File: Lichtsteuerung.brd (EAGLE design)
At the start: 157.7 x 86.4 mm, 180 parts, among them IC1 74HC595D, IC10 TSR_1-2450, IC11 MEGA64-A, IC12 75176AD, IC13 DS1307SO8, IC2 74HC595D, IC3 74HC595D, IC4 74HC595D, IC5 75176AD, IC6 MEGA8-AI, IC9 24FC128-I/SN, Q1 32.768, Q2 16MHz, Q3 16MHz, U1 MAX232SOIC16, X1 713-1410, X2 713-1410, X3 733-333, X5 713-1410, X6 733-334, X7 733-333, X8 733-333

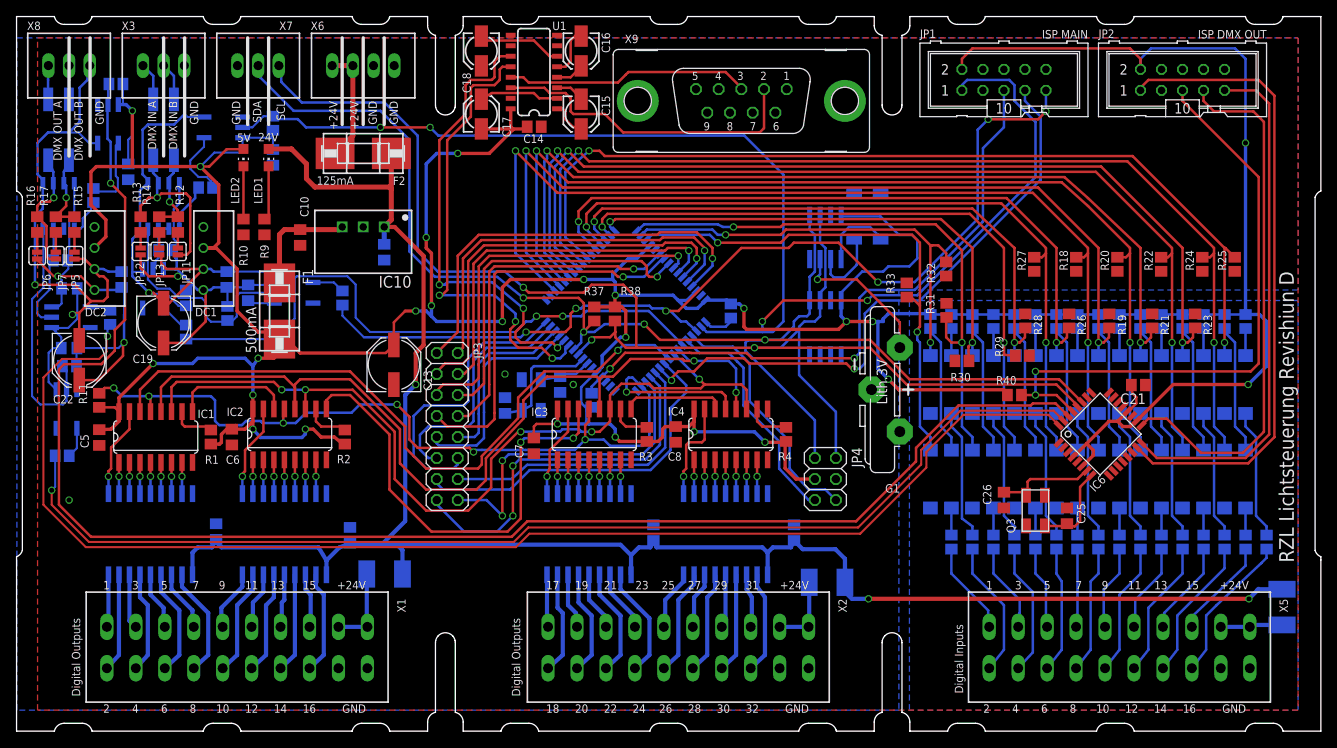
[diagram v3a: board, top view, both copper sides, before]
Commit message: Re-added smd jumpers, fixed silkscreens and added a few test points
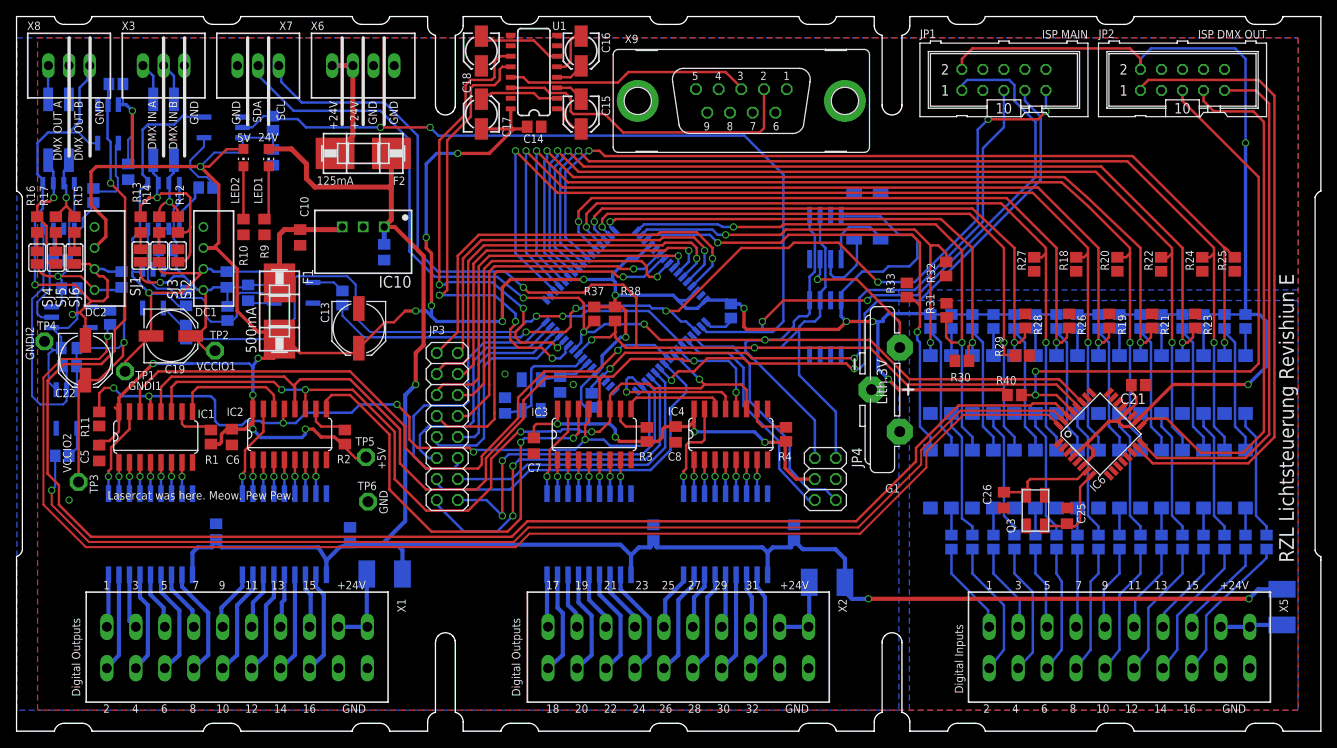
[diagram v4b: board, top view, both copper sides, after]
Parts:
- removed JP11, JP12, JP13, JP5, JP6, JP7: (no value), SparkFun:SJ_2S
- added SJ1, SJ2, SJ3, SJ4, SJ5, SJ6: (no value), jumper:SJ
- added TP1, TP2, TP3, TP4, TP5, TP6: TPPAD1-13, testpad:P1-13
- moved C13 6.11 mm to (41.4, 48.7), turned to 270 degrees
- moved R11 2.25 mm to (10.0, 37.8)
- moved C5 1.88 mm to (10.0, 33.6)
- moved C19 1.79 mm to (18.7, 47.8), turned to 0 degrees
- moved C22 0.75 mm to (8.33, 44.8)
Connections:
- removed net N$53: IC12.6, JP11.1, L1.1, R13.1
- removed net N$77: IC5.6, JP7.1, L2.1, R16.1
- removed net N$85: JP12.2, R13.2
- removed net N$86: JP13.1, R14.1
- removed net N$89: JP11.2, R12.1
- removed net N$91: JP5.1, R15.2
- removed net N$92: JP7.2, R17.1
- removed net N$94: JP6.2, R16.2
- new net TERM_A1: IC12.6, L1.1, R12.1, R13.1, SJ2.1
- new net TERM_A2: IC5.6, L2.1, R16.1, SJ5.1
- new net TERM_B1: SJ2.2
- new net TERM_B2: R17.1, SJ5.2
- new net TERM_HI1: R13.2, SJ1.2
- new net TERM_HI2: R16.2, SJ4.2
- new net TERM_LO1: R14.1, SJ3.2
- new net TERM_LO2: R15.2, SJ6.2
- net +5V: now also TP5.TP
- net GND: now also TP6.TP
- net GNDI1: now also SJ3.1, TP1.TP; no longer JP13.2
- net GNDI2: now also SJ6.1, TP4.TP; no longer JP5.2
- net VCCIO1: now also SJ1.1, TP2.TP; no longer JP12.1
- net VCCIO2: now also SJ4.1, TP3.TP; no longer JP6.1
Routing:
- net TERM_A1: track 0.00 -> 23.3 mm, vias 0 -> 1
- net N$53: track 21.2 -> 0.00 mm, vias 1 -> 0
- net TERM_A2: track 0.00 -> 15.5 mm, vias 0 -> 1
- net N$77: track 14.9 -> 0.00 mm, vias 1 -> 0
- net VCCIO2: track 55.5 -> 67.7 mm
- net GNDI1: track 76.5 -> 86.4 mm
- net N$94: track 2.39 -> 0.00 mm
- net N$92: track 2.39 -> 0.00 mm
- net N$91: track 2.39 -> 0.00 mm
- net TERM_LO2: track 0.00 -> 2.29 mm
- net TERM_HI2: track 0.00 -> 2.29 mm
- net TERM_B2: track 0.00 -> 2.29 mm
- net OE: track 108.6 -> 110.9 mm
- net TERM_LO1: track 0.00 -> 2.04 mm
- net TERM_HI1: track 0.00 -> 2.04 mm
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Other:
- board text added: "+5V"
- board text added: "GNDI1"
- board text added: "GNDI2"
- board text added: "Lasercat was here. Meow. Pew Pew."
- board text added: "RZL Lichtsteuerung Revishiun E"
- board text added: "VCCIO1"
- board text added: "VCCIO2"
- board text removed: "RZL Lichtsteuerung Revishiun D"

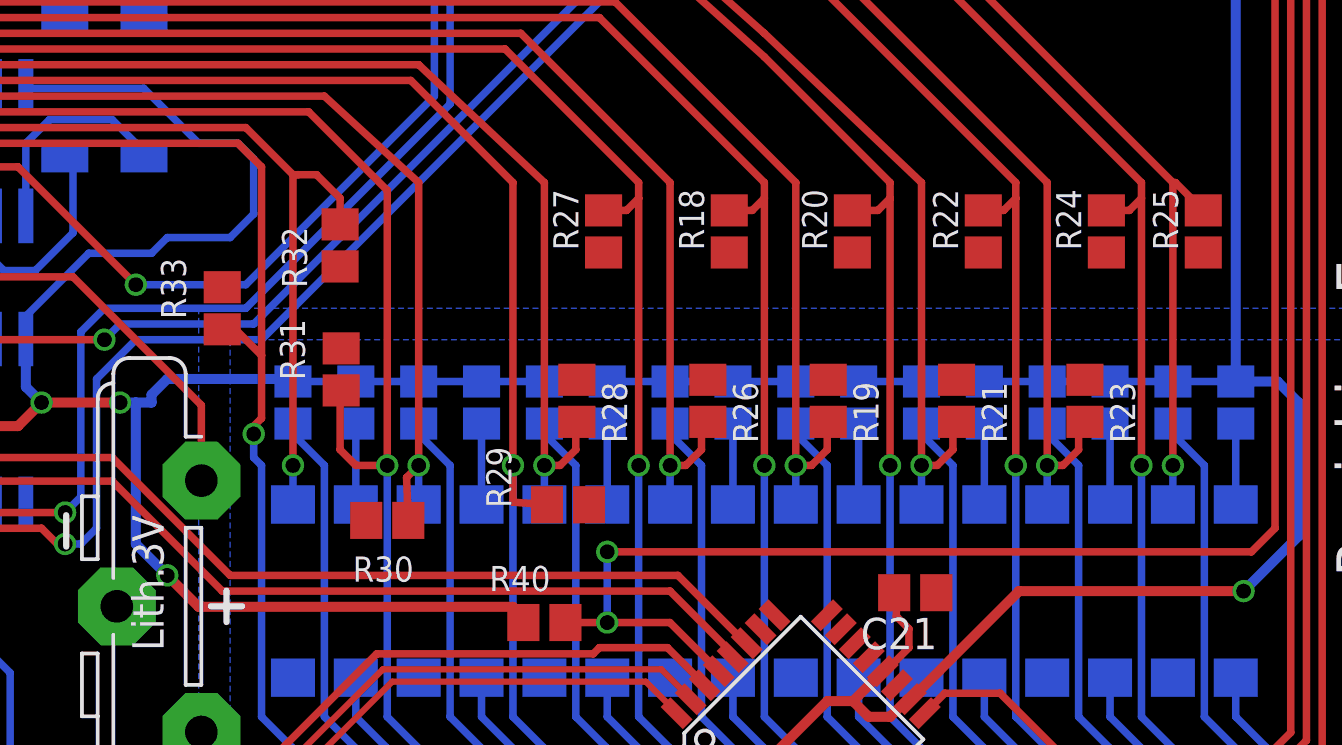
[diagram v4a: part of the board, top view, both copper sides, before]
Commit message: Added reichelt ordercodes
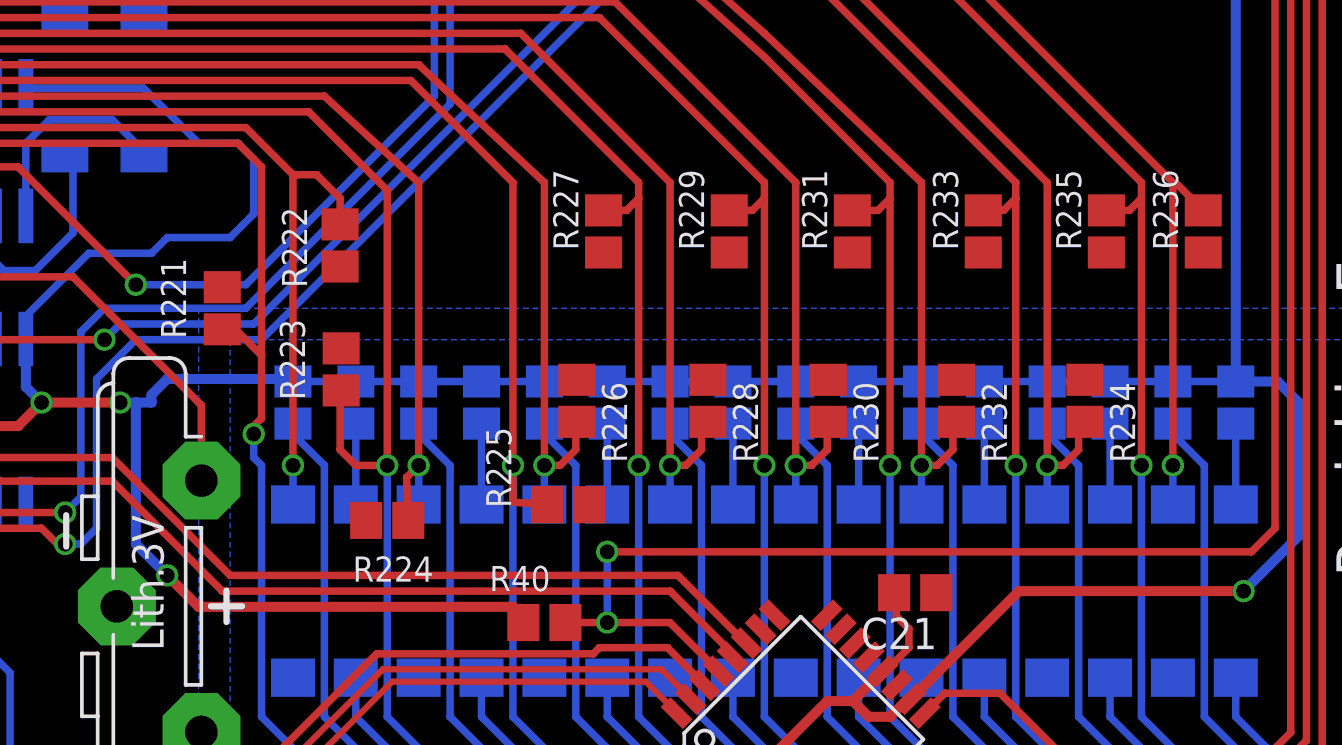
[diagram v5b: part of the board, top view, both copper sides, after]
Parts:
- renumbered R18 to R229, R19 to R230, R20 to R231, R21 to R232, R22 to R233, R23 to R234, R24 to R235, R25 to R236, R26 to R228, R27 to R227, R28 to R226, R29 to R225, R30 to R224, R31 to R223, R32 to R222, R33 to R221

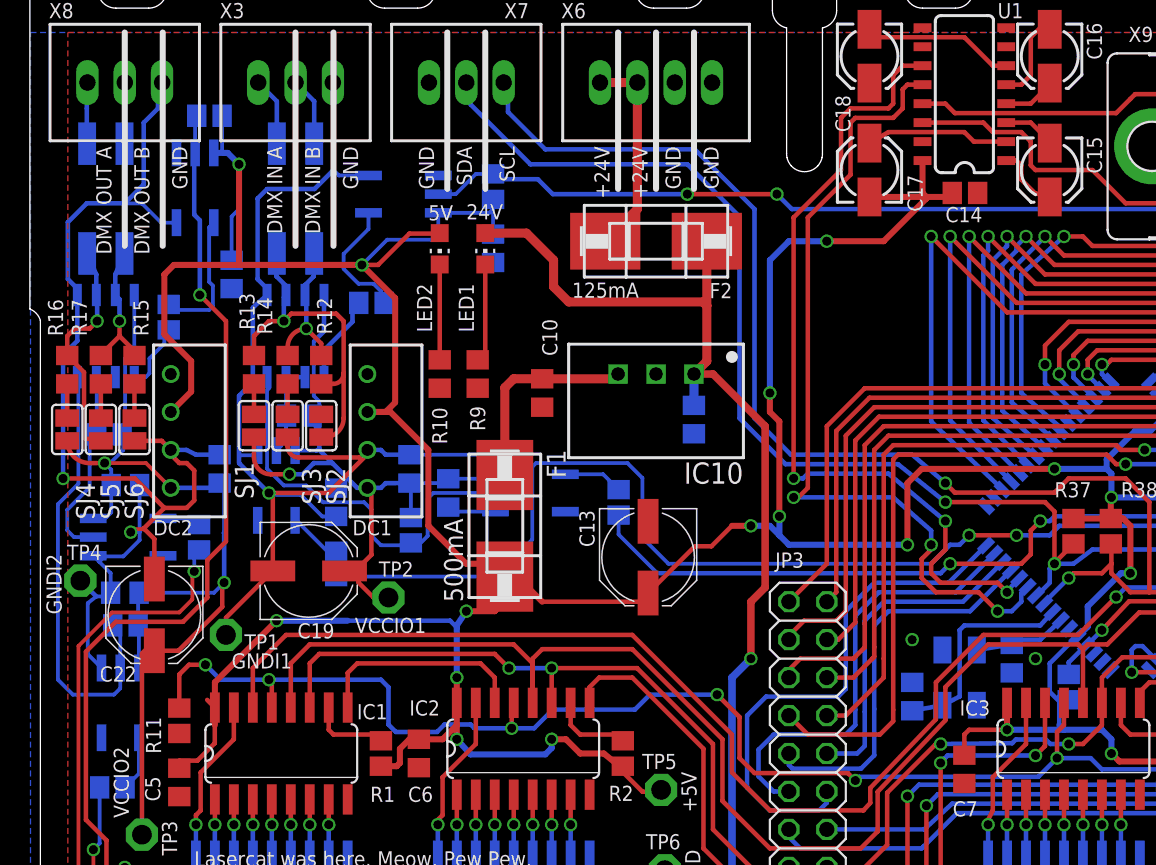
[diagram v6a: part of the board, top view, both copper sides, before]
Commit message: Fixed ACPL-M50L footprint size
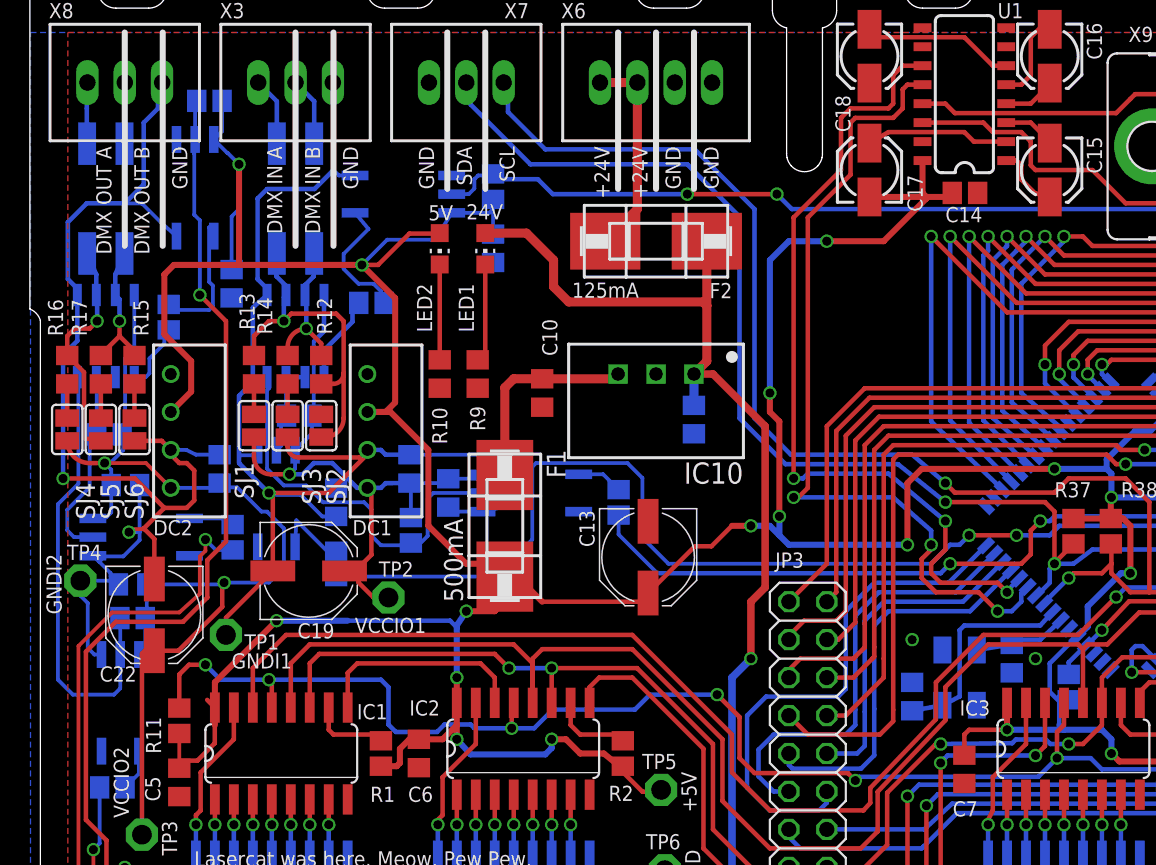
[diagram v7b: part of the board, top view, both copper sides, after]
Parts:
- moved R7 2.25 mm to (13.6, 50.0)
- moved R45 1.00 mm to (12.0, 79.2)
- moved OK1 0.88 mm to (7.45, 50.0)
- moved OK32 0.88 mm to (16.5, 52.6)
- moved C28 0.76 mm to (6.88, 46.9)
- moved R44 0.69 mm to (6.88, 44.6)
- moved C30 0.62 mm to (13.5, 67.0)
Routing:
- net VCCIO2: track 67.7 -> 72.9 mm
- net RE/DE2: track 160.9 -> 164.0 mm
- net +5V: track 573.7 -> 576.1 mm
- net VCCIO1: track 48.1 -> 46.2 mm
- net N$133: track 3.61 -> 5.30 mm
- net DMX_O_R: track 190.9 -> 191.8 mm
- net GNDI1: track 86.4 -> 85.5 mm
- net RE_OUT: track 7.42 -> 6.46 mm
- net N$73: track 3.71 -> 2.81 mm
- net N$116: track 3.99 -> 3.09 mm
- net GNDI2: track 80.6 -> 81.3 mm
- net RXD/MOSI: track 158.6 -> 158.0 mm
- net N$79: track 2.53 -> 3.05 mm

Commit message: Changed pulldown resistors from 10k to 47k for the input optocouplers
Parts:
- R221, R222, R223, R224, R225, R226, R227, R228, R229, R230, R231, R232, R233, R234, R235, R236: value 10k -> 47k
